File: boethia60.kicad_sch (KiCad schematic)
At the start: 9 parts, among them SW1 SW_Push_Reset, U1 RP2040, U2 NCP1117-3.3_SOT223

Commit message: Everything is coming together.
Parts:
- removed R3: 10k, symbol Device:R
- added C1, C4: 22p, Capacitor_SMD:C_0805_2012Metric, symbol Device:C
- added C10, C11, C12, C14, C15, C16, C6, C7, C8, C9: 100n, Capacitor_SMD:C_0805_2012Metric, symbol Device:C
- added C13, C5: 1u, Capacitor_SMD:C_0805_2012Metric, symbol Device:C
- added F1: 500m, Fuse:Fuse_1206_3216Metric, symbol Device:Polyfuse_Small
- added FB1: 60@100MHz, Inductor_SMD:L_0805_2012Metric, symbol Device:FerriteBead_Small
- added J1: Conn_01x06, random-keyboard-parts:Reset_Pretty-Mask, symbol Connector_Generic:Conn_01x06
- added R1, R2, R7: 1k, Resistor_SMD:R_0805_2012Metric, symbol Device:R
- added R5, R6: 5.1k, Resistor_SMD:R_0805_2012Metric, symbol Device:R
- added U2: PRTR5V0U2X, random-keyboard-parts:SOT143B, symbol random-keyboard-parts:PRTR5V0U2X
- added U4: W25Q128JVS, Package_SO:SOIC-8_5.23x5.23mm_P1.27mm, symbol Memory_Flash:W25Q128JVS
- added Y1: Crystal_GND24_Small, Crystal:Crystal_SMD_3225-4Pin_3.2x2.5mm, symbol Device:Crystal_GND24_Small
- C2: renamed from C1; footprint (none) -> Capacitor_SMD:C_0805_2012Metric
- C3: renamed from C2; footprint (none) -> Capacitor_SMD:C_0805_2012Metric
- R3: renamed from R1; value 22 -> 27.4; footprint (none) -> Resistor_SMD:R_0805_2012Metric
- R4: renamed from R2; value 22 -> 27.4; footprint (none) -> Resistor_SMD:R_0805_2012Metric
- SW1: value SW_Push_Reset -> SW_Push; footprint (none) -> Button_Switch_SMD:SW_SPST_SKQG_WithStem
- USB1: footprint (none) -> Type-C:HRO-TYPE-C-31-M-12-HandSoldering
- renumbered U2 to U1, U1 to U3
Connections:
- net +3V3: now also U3.1 (IOVDD), U3.10 (IOVDD), U3.22 (IOVDD), U3.33 (IOVDD), U3.42 (IOVDD), U3.43 (ADC_AVDD), U3.44 (VREG_IN), U3.48 (USB_VDD), U3.49 (IOVDD), C10.1, C11.1, C12.1, C16.1, C5.1, C6.1, C7.1, C8.1, C9.1, J1.2 (Pin_2), R1.1, U4.8 (VCC)
- net GND: now also U3.19 (TESTEN), U3.57 (GND), USB1.1 (GND), USB1.12 (GND), USB1.13 (SHIELD), C1.1, C10.2, C11.2, C12.2, C13.2, C14.2, C15.2, C16.2, C4.1, C5.2, C6.2, C7.2, C8.2, C9.2, FB1.2, J1.6 (Pin_6), R5.2, R6.2, U2.1 (GND), U4.4 (GND), Y1.2, Y1.4
- net VBUS: now also F1.1; no longer C2.1, U1.3 (VI)
- net DP: now reaches R4.2, USB1.6 (DP1), USB1.8 (DP2)
- net DP: now also U2.2 (IO1)
- net col7: now reaches U3.11 (GPIO8)
- net col8: now reaches U3.12 (GPIO9)
- net col9: now reaches U3.13 (GPIO10)
- net row4: now reaches U3.14 (GPIO11)
- net row3: now reaches U3.15 (GPIO12)
- net row2: now reaches U3.16 (GPIO13)
- net row1: now reaches U3.17 (GPIO14)
- net row0: now reaches U3.18 (GPIO15)
- net GPIO0: now reaches U3.2 (GPIO0)
- net XIN: now reaches U3.20 (XIN)
- net XIN: now also C1.2, Y1.1
- net XOUT: now reaches U3.21 (XOUT)
- net XOUT: now also R2.2
- net +1V1: now reaches U3.23 (DVDD), U3.50 (DVDD)
- net +1V1: now also U3.45 (VREG_VOUT), C13.1, C14.1, C15.1
- net SWCLK: now reaches U3.24 (SWCLK)
- net SWCLK: now also J1.3 (Pin_3)
- net SWD: now reaches U3.25 (SWD)
- net SWD: now also J1.4 (Pin_4)
- net RUN: now reaches U3.26 (RUN)
- net RUN: now also J1.5 (Pin_5), R1.2
- net col6: now reaches U3.27 (GPIO16)
- net col10: now reaches U3.28 (GPIO17)
- net col11: now reaches U3.29 (GPIO18)
- net GPIO1: now reaches U3.3 (GPIO1)
- net col12: now reaches U3.30 (GPIO19)
- net col13: now reaches U3.31 (GPIO20)
- net col14: now reaches U3.32 (GPIO21)
- net col0: now reaches U3.34 (GPIO22)
- net col1: now reaches U3.35 (GPIO23)
- net col2: now reaches U3.36 (GPIO24)
- net GPIO25: now reaches U3.37 (GPIO25)
- net GPIO26: now reaches U3.38 (GPIO26_ADC0)
- net GPIO27: now reaches U3.39 (GPIO27_ADC1)
- net GPIO2: now reaches U3.4 (GPIO2)
- net GPIO28: now reaches U3.40 (GPIO28_ADC2)
- net GPIO29: now reaches U3.41 (GPIO29_ADC3)
- net GPIO3: now reaches U3.5 (GPIO3)
- net SD3: now reaches U3.51 (QSPI_SD3)
- net SD3: now also U4.7 (IO3)
- net SCLK: now reaches U3.52 (QSPI_SCLK)
- net SCLK: now also U4.6 (CLK)
- net SD0: now reaches U3.53 (QSPI_SD0)
- net SD0: now also U4.5 (DI(IO0))
- net SD2: now reaches U3.54 (QSPI_SD2)
- net SD2: now also U4.3 (IO2)
- net SD1: now reaches U3.55 (QSPI_SD1)
- net SD1: now also U4.2 (DO(IO1))
- net CS: now reaches U3.56 (QSPI_SS)
- net CS: now also R7.2, U4.1 (~{CS})
- net GPIO4: now reaches U3.6 (GPIO4)
- net col3: now reaches U3.7 (GPIO5)
- net col4: now reaches U3.8 (GPIO6)
- net col5: now reaches U3.9 (GPIO7)
- net at USB1.10 (CC2): now also R5.1
- net at USB1.4 (CC1): now also R6.1
- net DN: now reaches R3.1, USB1.5 (DN2), USB1.7 (DN1)
- net DN: now also U2.3 (IO2)
- net RESET: no longer names the net of SW1.2
- net RESET: now also R7.1
- new net: C4.2, R2.1, Y1.3
- new net +5V: C2.1, F1.2, U1.3 (VI), U2.4 (VCC)
- new net Earth: FB1.1
- no-connect marks 2 -> 3
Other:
- added sheet matrix (matrix.kicad_sch)
- note added: "Crystal"
- note added: "Flash"
- note added: "Voltage Regulator"
- moved on the sheet: C2, C3, R3, R4, U1, U3, USB1

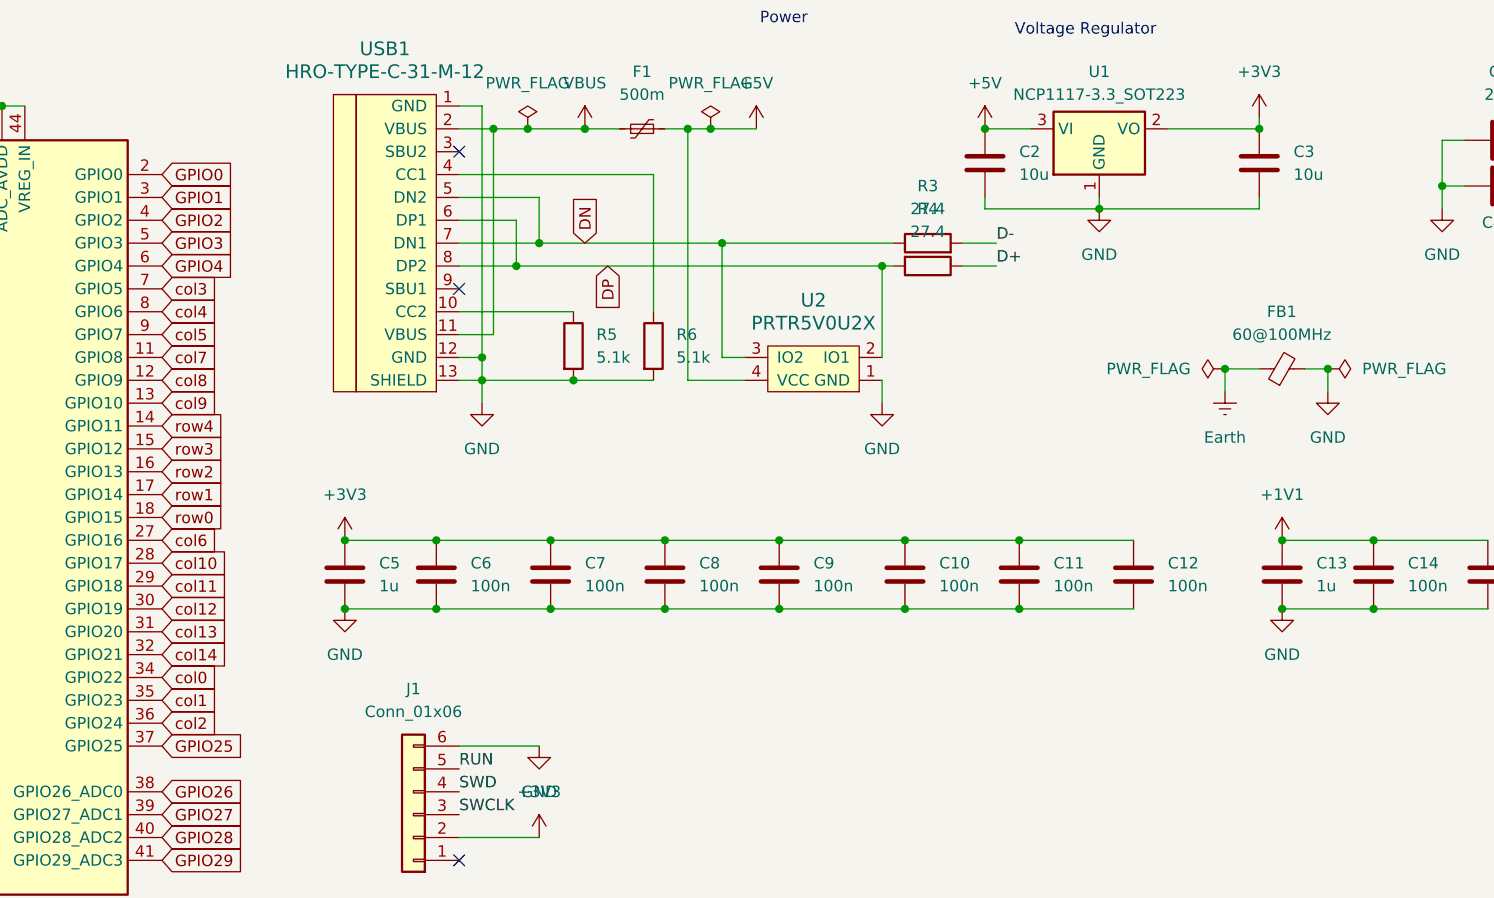
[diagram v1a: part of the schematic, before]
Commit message: Change footprints, fix errors, WIP BOM.
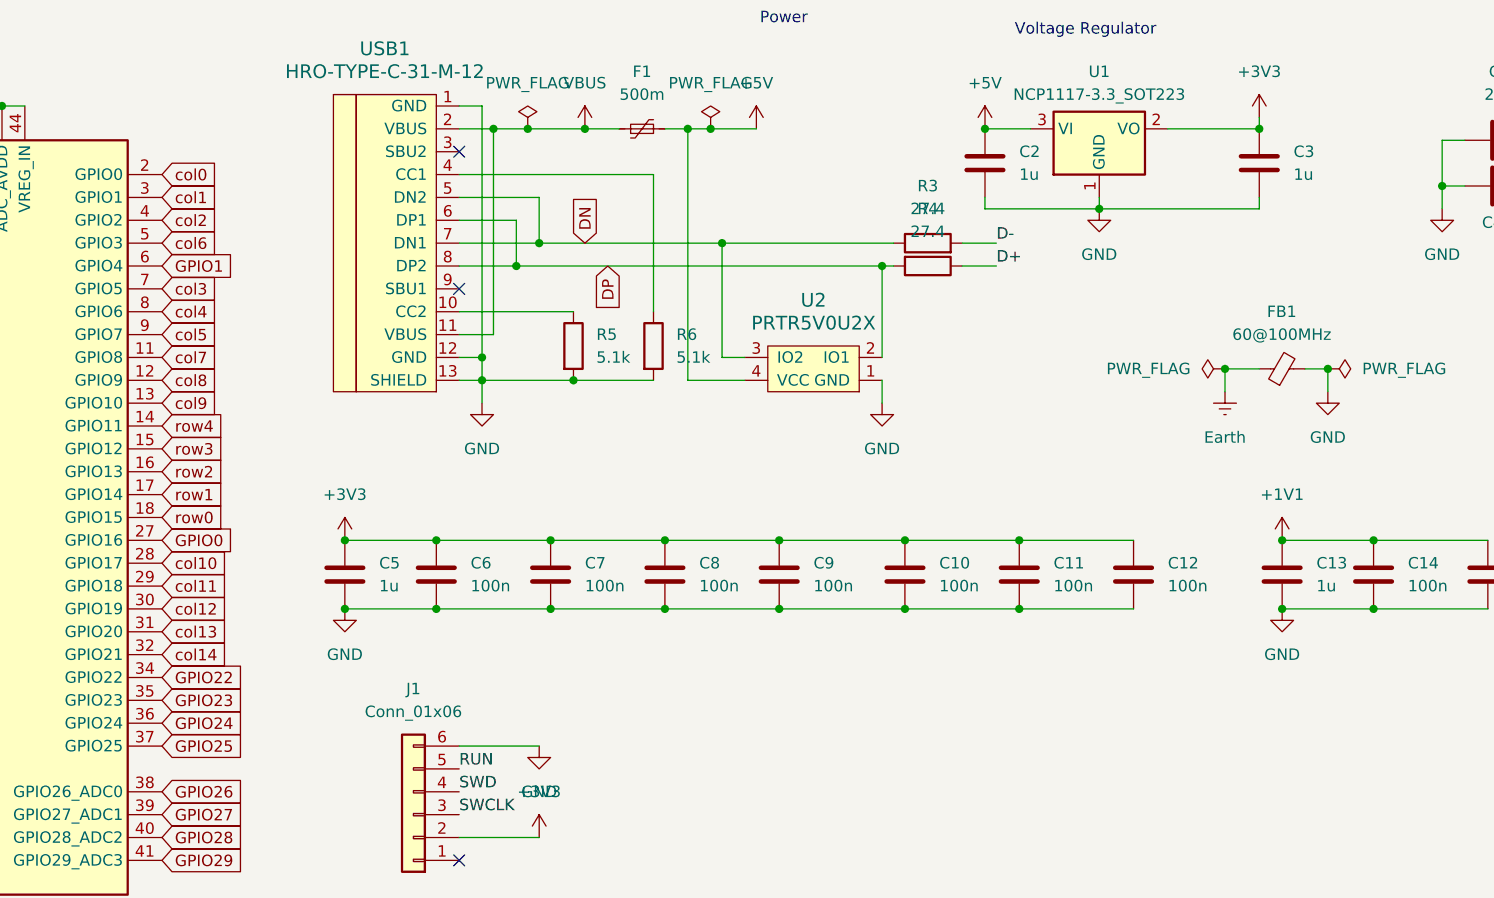
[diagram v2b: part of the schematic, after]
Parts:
- C1, C4: footprint Capacitor_SMD:C_0805_2012Metric -> Capacitor_SMD:C_0402_1005Metric; JLCPCB Part (none) -> C106203
- C10, C11, C12, C14, C15, C16, C6, C7, C8, C9: footprint Capacitor_SMD:C_0805_2012Metric -> Capacitor_SMD:C_0402_1005Metric; JLCPCB Part (none) -> C169292
- C13, C5: footprint Capacitor_SMD:C_0805_2012Metric -> Capacitor_SMD:C_0402_1005Metric; JLCPCB Part (none) -> C15684
- C2, C3: value 10u -> 1u; footprint Capacitor_SMD:C_0805_2012Metric -> Capacitor_SMD:C_0402_1005Metric; JLCPCB Part (none) -> C15684
- F1: footprint Fuse:Fuse_1206_3216Metric -> Fuse_0805_2012Metric; JLCPCB Part (none) -> C2833485
- FB1: footprint Inductor_SMD:L_0805_2012Metric -> Inductor_SMD:L_0603_1608Metric; JLCPCB Part (none) -> C14709
- R1, R2, R7: footprint Resistor_SMD:R_0805_2012Metric -> R_0402_1005Metric; JLCPCB Part (none) -> C17513
- R3, R4: footprint Resistor_SMD:R_0805_2012Metric -> R_0402_1005Metric; JLCPCB Part (none) -> C17588
- R5, R6: footprint Resistor_SMD:R_0805_2012Metric -> R_0402_1005Metric; JLCPCB Part (none) -> C84375
- SW1: JLCPCB Part (none) -> C318884
- U1: JLCPCB Part (none) -> XC6206
- U2: JLCPCB Part (none) -> C2827688
- U3: JLCPCB Part (none) -> C2040
- U4: JLCPCB Part (none) -> C82317
- Y1: JLCPCB Part (none) -> C9002
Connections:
- net GPIO2 is gone; now on net col2: U3.4 (GPIO2)
- net GPIO3 is gone; now on net col6: U3.5 (GPIO3)
- net GPIO4 is gone; now on net GPIO1: U3.6 (GPIO4)
- net GPIO0: now also U3.27 (GPIO16); no longer U3.2 (GPIO0)
- net GPIO1: no longer U3.3 (GPIO1)
- net col0: now also U3.2 (GPIO0); no longer U3.34 (GPIO22)
- net col1: now also U3.3 (GPIO1); no longer U3.35 (GPIO23)
- net col2: no longer U3.36 (GPIO24)
- net col6: no longer U3.27 (GPIO16)
- new net GPIO22: U3.34 (GPIO22)
- new net GPIO23: U3.35 (GPIO23)
- new net GPIO24: U3.36 (GPIO24)

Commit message: Fix firmware pins.
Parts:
- C1, C4: JLCPCB Part C106203 -> C1555
- C10, C11, C12, C14, C15, C16, C6, C7, C8, C9: JLCPCB Part C169292 -> C14663
- C13, C2, C3, C5: JLCPCB Part C15684 -> C52923
- F1: JLCPCB Part C2833485 -> C1015
- R1, R2, R7: JLCPCB Part C17513 -> C11702
- R3, R4: JLCPCB Part C17588 -> C274349
- R5, R6: JLCPCB Part C84375 -> C25905
- U1: footprint Package_TO_SOT_SMD:SOT-223-3_TabPin2 -> Package_TO_SOT_SMD:SOT-23-3; JLCPCB Part XC6206 -> C5446
- U2: footprint random-keyboard-parts:SOT143B -> Package_TO_SOT_SMD:SOT-143
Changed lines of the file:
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@@
 			)
 		)
-		(property "JLCPCB Part" "C169292"
+		(property "JLCPCB Part" "C14663"
 			(at 229.87 80.01 0)
 			(effects
@@
 			)
 		)
-		(property "JLCPCB Part" "C169292"
+		(property "JLCPCB Part" "C14663"
 			(at 217.17 80.01 0)
 			(effects
@@
 			)
 		)
-		(property "JLCPCB Part" "C169292"
+		(property "JLCPCB Part" "C14663"
 			(at 125.73 80.01 0)
 			(effects
@@
 			)
 		)
-		(property "JLCPCB Part" "C169292"
+		(property "JLCPCB Part" "C14663"
 			(at 113.03 80.01 0)
 			(effects
@@
 			)
 		)
-		(property "JLCPCB Part" "C15684"
+		(property "JLCPCB Part" "C52923"
 			(at 173.99 34.29 0)
 			(effects
@@
 			)
 		)
-		(property "JLCPCB Part" "C15684"
+		(property "JLCPCB Part" "C52923"
 			(at 102.87 80.01 0)
 			(effects
@@
 			)
 		)
-		(property "Footprint" "Package_TO_SOT_SMD:SOT-223-3_TabPin2"
+		(property "Footprint" "Package_TO_SOT_SMD:SOT-23-3"
 			(at 186.69 25.4 0)
 			(effects
@@
 			)
 		)
-		(property "JLCPCB Part" "XC6206"
+		(property "JLCPCB Part" "C5446"
 			(at 186.69 30.48 0)
 			(effects
@@
 			)
 		)
-		(property "JLCPCB Part" "C106203"
+		(property "JLCPCB Part" "C1555"
 			(at 231.14 31.75 0)
 			(effects
@@
 			)
 		)
-		(property "JLCPCB Part" "C2833485"
+		(property "JLCPCB Part" "C1015"
 			(at 135.89 30.48 0)
 			(effects
@@
 			)
 		)
-		(property "JLCPCB Part" "C169292"
+		(property "JLCPCB Part" "C14663"
 			(at 261.62 121.92 0)
 			(effects
@@
 			)
 		)
-		(property "JLCPCB Part" "C169292"
+		(property "JLCPCB Part" "C14663"
 			(at 177.8 80.01 0)
 			(effects
@@
 			)
 		)
-		(property "JLCPCB Part" "C17588"
+		(property "JLCPCB Part" "C274349"
 			(at 167.64 45.72 0)
 			(effects
@@
 			)
 		)
-		(property "JLCPCB Part" "C15684"
+		(property "JLCPCB Part" "C52923"
 			(at 207.01 80.01 0)
 			(effects
@@
 			)
 		)
-		(property "Footprint" "random-keyboard-parts:SOT143B"
+		(property "Footprint" "Package_TO_SOT_SMD:SOT-143"
 			(at 154.94 57.15 0)
 			(effects
@@
 			)
 		)
-		(property "JLCPCB Part" "C17513"
+		(property "JLCPCB Part" "C11702"
 			(at 256.54 36.83 0)
 			(effects
@@
 			)
 		)
-		(property "JLCPCB Part" "C15684"
+		(property "JLCPCB Part" "C52923"
 			(at 204.47 34.29 0)
 			(effects
@@
 			)
 		)
-		(property "JLCPCB Part" "C84375"
+		(property "JLCPCB Part" "C25905"
 			(at 137.16 54.61 0)
 			(effects
@@
 			)
 		)
-		(property "JLCPCB Part" "C17513"
+		(property "JLCPCB Part" "C11702"
 			(at 232.41 132.08 0)
 			(effects
@@
 			)
 		)
-		(property "JLCPCB Part" "C169292"
+		(property "JLCPCB Part" "C14663"
 			(at 138.43 80.01 0)
 			(effects
@@
 			)
 		)
-		(property "JLCPCB Part" "C17588"
+		(property "JLCPCB Part" "C274349"
 			(at 167.64 43.18 0)
 			(effects
@@
 			)
 		)
-		(property "JLCPCB Part" "C84375"
+		(property "JLCPCB Part" "C25905"
 			(at 128.27 54.61 0)
 			(effects
@@
 			)
 		)
-		(property "JLCPCB Part" "C17513"
+		(property "JLCPCB Part" "C11702"
 			(at 30.48 27.94 0)
 			(effects
@@
 			)
 		)
-		(property "JLCPCB Part" "C169292"
+		(property "JLCPCB Part" "C14663"
 			(at 151.13 80.01 0)
 			(effects
@@
 			)
 		)
-		(property "JLCPCB Part" "C169292"
+		(property "JLCPCB Part" "C14663"
 			(at 190.5 80.01 0)
 			(effects
@@
 			)
 		)
-		(property "JLCPCB Part" "C169292"
+		(property "JLCPCB Part" "C14663"
 			(at 165.1 80.01 0)
 			(effects
@@
 			)
 		)
-		(property "JLCPCB Part" "C106203"
+		(property "JLCPCB Part" "C1555"
 			(at 231.14 36.83 0)
 			(effects
